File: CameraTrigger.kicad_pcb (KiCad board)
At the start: 2 copper layers, 2 parts, among them U1 LCD-016N002L

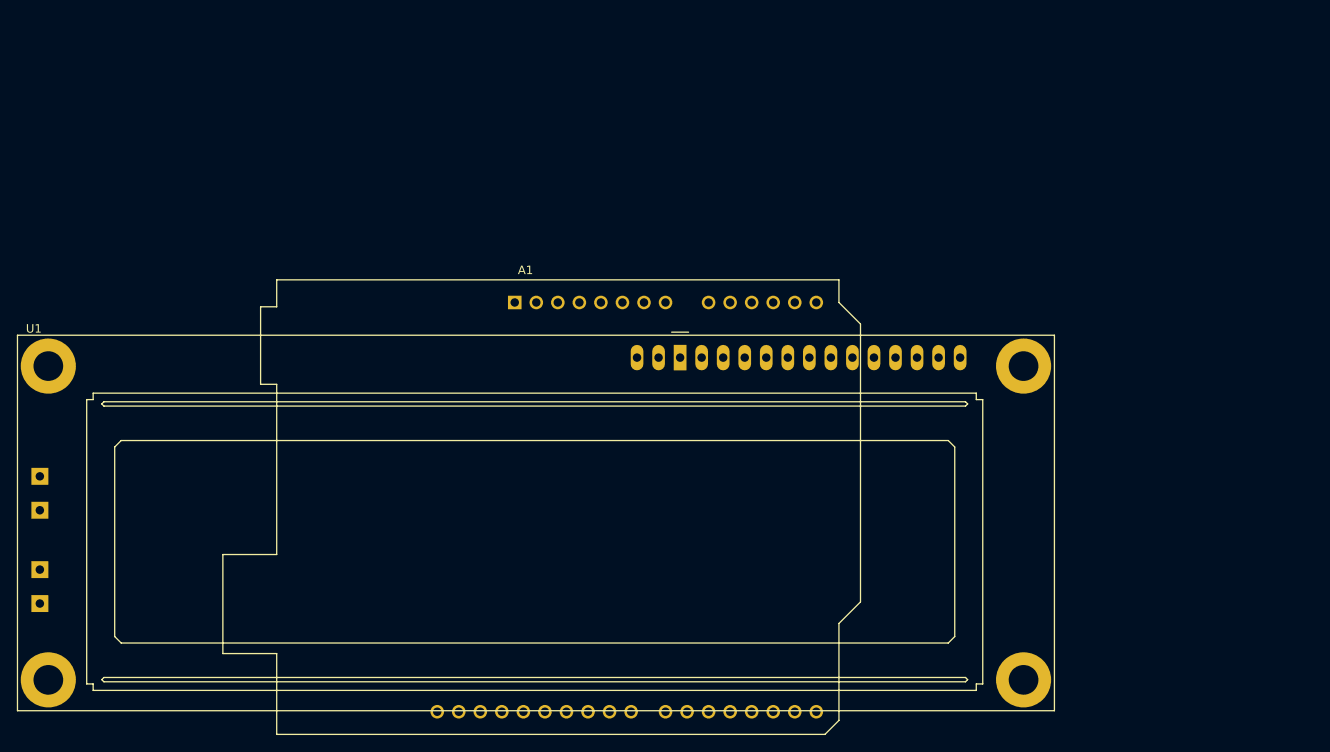
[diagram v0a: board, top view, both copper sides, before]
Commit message: Add final sensors and triggering mechanisms
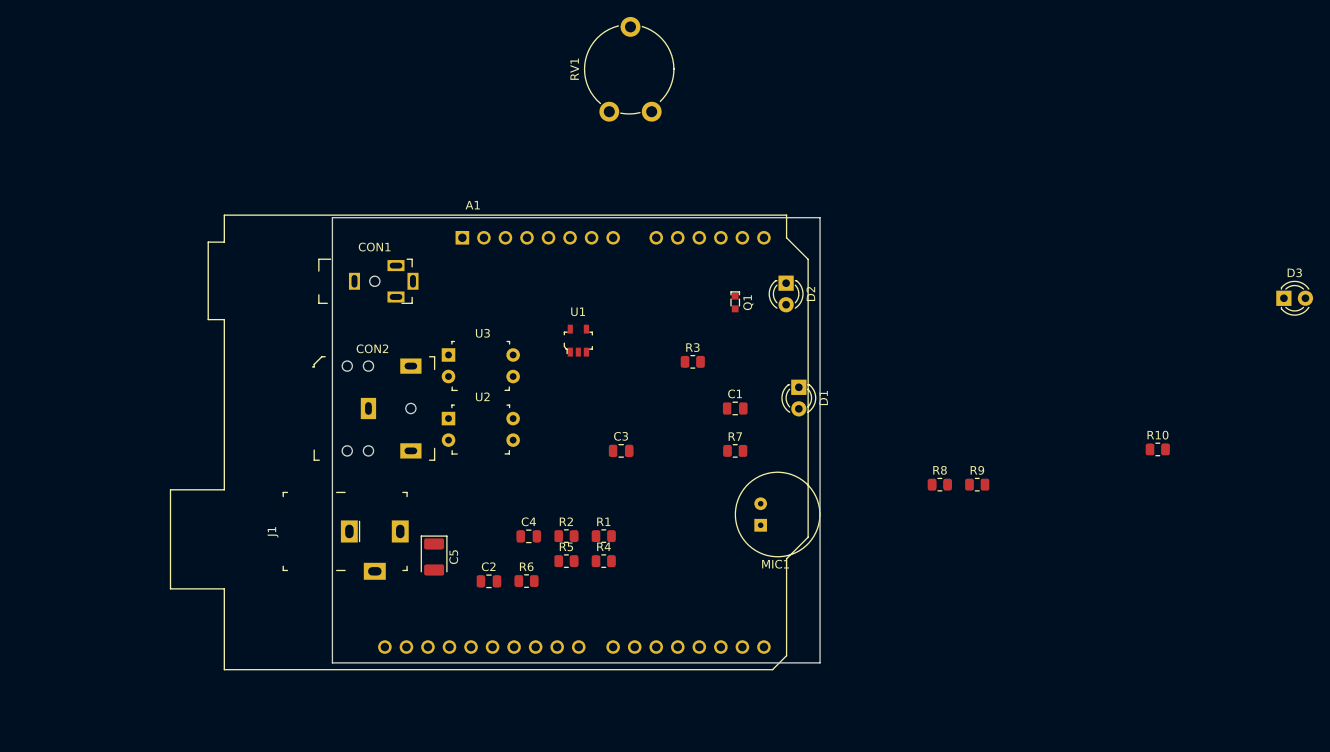
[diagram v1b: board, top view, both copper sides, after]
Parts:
- added C1: 100 nF, Capacitor_SMD:C_0805_2012Metric, F.Cu at (160.0, 62.5)
- added C2: 10 nF, Capacitor_SMD:C_0805_2012Metric, F.Cu at (131.0, 82.9)
- added C3: 1uF, Capacitor_SMD:C_0805_2012Metric, F.Cu at (146.6, 67.5)
- added C4: 100pF, Capacitor_SMD:C_0805_2012Metric, F.Cu at (135.7, 77.6)
- added C5: C_Polarized_Small, Capacitor_Tantalum_SMD:CP_EIA-3528-15_AVX-H, F.Cu at (124.5, 80.0)
- added CON1: SJ1-2503A, digikey-footprints:Headphone_Jack_2.5mm_SJ1-2503A, F.Cu at (117.5, 47.5)
- added CON2: SJ1-3523N, digikey-footprints:Headphone_Jack_3.5mm_SJ1-3523N, F.Cu at (121.8, 62.5)
- added D1: LED, LED_THT:LED_D3.0mm, F.Cu at (167.5, 60.0)
- added D2: PD204-6C, LED_THT:LED_D3.0mm, F.Cu at (166.0, 47.7)
- added D3: LED, LED_THT:LED_D3.0mm, F.Cu at (224.7, 49.5)
- added J1: PJ-102A, digikey-footprints:Barrel_Jack_5.5mmODx2.1mmID_PJ-102A, F.Cu at (117.5, 77.0)
- added MIC1: CMA-4544PF-W, digikey-footprints:Mic_CMA-4544PF-W, F.Cu at (165.0, 75.0)
- added Q1: ALS-PT19-315C_L177_TR8, digikey-footprints:LED_2-SMD_No_Lead_1.7x0.8mm, F.Cu at (160.0, 50.0)
- added R1: 2k, Resistor_SMD:R_0805_2012Metric, F.Cu at (144.5, 77.5)
- added R10: 510, Resistor_SMD:R_0805_2012Metric, F.Cu at (209.8, 67.3)
- added R2: 2k, Resistor_SMD:R_0805_2012Metric, F.Cu at (140.1, 77.5)
- added R3: 1M, Resistor_SMD:R_0805_2012Metric, F.Cu at (155.0, 57.0)
- added R4: 1M, Resistor_SMD:R_0805_2012Metric, F.Cu at (144.5, 80.5)
- added R5: 10k, Resistor_SMD:R_0805_2012Metric, F.Cu at (140.1, 80.5)
- added R6: 100k, Resistor_SMD:R_0805_2012Metric, F.Cu at (135.4, 82.8)
- added R7: 7.5k, Resistor_SMD:R_0805_2012Metric, F.Cu at (160.0, 67.5)
- added R8: 4.7k, Resistor_SMD:R_0805_2012Metric, F.Cu at (184.1, 71.5)
- added R9: 510, Resistor_SMD:R_0805_2012Metric, F.Cu at (188.5, 71.5)
- added RV1: 10k, Potentiometer_THT:Potentiometer_Piher_PT-10-V10_Vertical, F.Cu at (150.2, 27.5)
- added U2: LTV-817, digikey-footprints:DIP-4_W7.62mm, F.Cu at (126.2, 63.7)
- added U3: LTV-817, digikey-footprints:DIP-4_W7.62mm, F.Cu at (126.2, 56.2)
- U1: value LCD-016N002L -> MAX4466EXK_T; footprint Display:LCD-016N002L -> digikey-footprints:SOT-353
- moved U1 12.2 mm to (141.5, 54.5)
- moved A1 9.82 mm to (127.8, 42.4)
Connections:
- A1 pad 10: unconnected-(A1-Pad10) -> LIGHT_SENS_INP
- A1 pad 11: unconnected-(A1-Pad11) -> LASER_SENS_INP
- A1 pad 17: unconnected-(A1-Pad17) -> FOCUS_TRIGGER
- A1 pad 18: unconnected-(A1-Pad18) -> SHUTTER_TRIGGER
- A1 pad 29: unconnected-(A1-Pad29) -> GND
- A1 pad 4: unconnected-(A1-Pad4) -> +3V3
- A1 pad 5: unconnected-(A1-Pad5) -> +5V
- A1 pad 6: unconnected-(A1-Pad6) -> GND
- A1 pad 7: unconnected-(A1-Pad7) -> GND
- A1 pad 8: unconnected-(A1-Pad8) -> +12V
- A1 pad 9: unconnected-(A1-Pad9) -> MIC_INP
- U1 pad 1: unconnected-(U1-Pad1) -> Net-(C2-Pad2)
- U1 pad 2: unconnected-(U1-Pad2) -> GND
- U1 pad 3: unconnected-(U1-Pad3) -> Net-(C4-Pad1)
- U1 pad 4: unconnected-(U1-Pad4) -> MIC_INP
- U1 pad 5: unconnected-(U1-Pad5) -> +5V
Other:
- board outline added: 57.5 x 52.5 mm
